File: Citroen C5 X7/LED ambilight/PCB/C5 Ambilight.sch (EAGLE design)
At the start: 21 parts, among them Q1 SQP90P06-07L_GE3, X1 2PIN_5MM_TERMINAL, X2 2PIN_5MM_TERMINAL, X3 JST-XH-03-PIN-ROUND-PAD

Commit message: Updated PCB
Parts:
- R2: value 12k -> 10k
- R3: value 470R -> 10k
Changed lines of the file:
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@@
 <grid distance="0.1" unitdist="inch" unit="inch" style="lines" multiple="1" display="no" altdistance="0.01" altunitdist="inch" altunit="inch"/>
 <layers>
-<layer number="1" name="Top" color="4" fill="1" visible="yes" active="no"/>
-<layer number="2" name="Route2" color="16" fill="1" visible="yes" active="no"/>
-<layer number="3" name="Route3" color="4" fill="3" visible="yes" active="no"/>
-<layer number="4" name="Route4" color="1" fill="4" visible="yes" active="no"/>
-<layer number="5" name="Route5" color="4" fill="4" visible="yes" active="no"/>
-<layer number="6" name="Route6" color="1" fill="8" visible="yes" active="no"/>
-<layer number="7" name="Route7" color="4" fill="8" visible="yes" active="no"/>
-<layer number="8" name="Route8" color="1" fill="2" visible="yes" active="no"/>
-<layer number="9" name="Route9" color="4" fill="2" visible="yes" active="no"/>
-<layer number="10" name="Route10" color="1" fill="7" visible="yes" active="no"/>
-<layer number="11" name="Route11" color="4" fill="7" visible="yes" active="no"/>
-<layer number="12" name="Route12" color="1" fill="5" visible="yes" active="no"/>
-<layer number="13" name="Route13" color="4" fill="5" visible="yes" active="no"/>
-<layer number="14" name="Route14" color="1" fill="6" visible="yes" active="no"/>
-<layer number="15" name="Route15" color="23" fill="1" visible="yes" active="no"/>
-<layer number="16" name="Bottom" color="1" fill="1" visible="yes" active="no"/>
-<layer number="17" name="Pads" color="2" fill="1" visible="yes" active="no"/>
-<layer number="18" name="Vias" color="2" fill="1" visible="yes" active="no"/>
-<layer number="19" name="Unrouted" color="6" fill="1" visible="yes" active="no"/>
-<layer number="20" name="Dimension" color="24" fill="1" visible="yes" active="no"/>
-<layer number="21" name="tPlace" color="7" fill="1" visible="yes" active="no"/>
-<layer number="22" name="bPlace" color="7" fill="1" visible="yes" active="no"/>
-<layer number="23" name="tOrigins" color="15" fill="1" visible="yes" active="no"/>
-<layer number="24" name="bOrigins" color="15" fill="1" visible="yes" active="no"/>
-<layer number="25" name="tNames" color="7" fill="1" visible="yes" active="no"/>
-<layer number="26" name="bNames" color="7" fill="1" visible="yes" active="no"/>
-<layer number="27" name="tValues" color="7" fill="1" visible="yes" active="no"/>
-<layer number="28" name="bValues" color="7" fill="1" visible="yes" active="no"/>
+<layer number="1" name="Top" color="4" fill="1" visible="no" active="no"/>
+<layer number="2" name="Route2" color="16" fill="1" visible="no" active="no"/>
+<layer number="3" name="Route3" color="4" fill="3" visible="no" active="no"/>
+<layer number="4" name="Route4" color="1" fill="4" visible="no" active="no"/>
+<layer number="5" name="Route5" color="4" fill="4" visible="no" active="no"/>
+<layer number="6" name="Route6" color="1" fill="8" visible="no" active="no"/>
+<layer number="7" name="Route7" color="4" fill="8" visible="no" active="no"/>
+<layer number="8" name="Route8" color="1" fill="2" visible="no" active="no"/>
+<layer number="9" name="Route9" color="4" fill="2" visible="no" active="no"/>
+<layer number="10" name="Route10" color="1" fill="7" visible="no" active="no"/>
+<layer number="11" name="Route11" color="4" fill="7" visible="no" active="no"/>
+<layer number="12" name="Route12" color="1" fill="5" visible="no" active="no"/>
+<layer number="13" name="Route13" color="4" fill="5" visible="no" active="no"/>
+<layer number="14" name="Route14" color="1" fill="6" visible="no" active="no"/>
+<layer number="15" name="Route15" color="23" fill="1" visible="no" active="no"/>
+<layer number="16" name="Bottom" color="1" fill="1" visible="no" active="no"/>
+<layer number="17" name="Pads" color="2" fill="1" visible="no" active="no"/>
+<layer number="18" name="Vias" color="2" fill="1" visible="no" active="no"/>
+<layer number="19" name="Unrouted" color="6" fill="1" visible="no" active="no"/>
+<layer number="20" name="Dimension" color="24" fill="1" visible="no" active="no"/>
+<layer number="21" name="tPlace" color="7" fill="1" visible="no" active="no"/>
+<layer number="22" name="bPlace" color="7" fill="1" visible="no" active="no"/>
+<layer number="23" name="tOrigins" color="15" fill="1" visible="no" active="no"/>
+<layer number="24" name="bOrigins" color="15" fill="1" visible="no" active="no"/>
+<layer number="25" name="tNames" color="7" fill="1" visible="no" active="no"/>
+<layer number="26" name="bNames" color="7" fill="1" visible="no" active="no"/>
+<layer number="27" name="tValues" color="7" fill="1" visible="no" active="no"/>
+<layer number="28" name="bValues" color="7" fill="1" visible="no" active="no"/>
 <layer number="29" name="tStop" color="7" fill="3" visible="no" active="no"/>
 <layer number="30" name="bStop" color="7" fill="6" visible="no" active="no"/>
@@
 <layer number="35" name="tGlue" color="7" fill="4" visible="no" active="no"/>
 <layer number="36" name="bGlue" color="7" fill="5" visible="no" active="no"/>
-<layer number="37" name="tTest" color="7" fill="1" visible="yes" active="no"/>
-<layer number="38" name="bTest" color="7" fill="1" visible="yes" active="no"/>
+<layer number="37" name="tTest" color="7" fill="1" visible="no" active="no"/>
+<layer number="38" name="bTest" color="7" fill="1" visible="no" active="no"/>
 <layer number="39" name="tKeepout" color="4" fill="11" visible="no" active="no"/>
 <layer number="40" name="bKeepout" color="1" fill="11" visible="no" active="no"/>
@@
 <layer number="44" name="Drills" color="7" fill="1" visible="no" active="no"/>
 <layer number="45" name="Holes" color="7" fill="1" visible="no" active="no"/>
-<layer number="46" name="Milling" color="3" fill="1" visible="yes" active="no"/>
-<layer number="47" name="Measures" color="7" fill="1" visible="yes" active="no"/>
-<layer number="48" name="Document" color="7" fill="1" visible="yes" active="no"/>
-<layer number="49" name="Reference" color="7" fill="1" visible="yes" active="no"/>
-<layer number="50" name="dxf" color="7" fill="1" visible="yes" active="no"/>
-<layer number="51" name="tDocu" color="7" fill="1" visible="yes" active="no"/>
-<layer number="52" name="bDocu" color="7" fill="1" visible="yes" active="no"/>
-<layer number="53" name="tGND_GNDA" color="7" fill="9" visible="yes" active="no"/>
-<layer number="54" name="bGND_GNDA" color="1" fill="9" visible="yes" active="no"/>
-<layer number="56" name="wert" color="7" fill="1" visible="yes" active="no"/>
-<layer number="57" name="tCAD" color="7" fill="1" visible="yes" active="no"/>
-<layer number="59" name="tCarbon" color="7" fill="1" visible="yes" active="no"/>
-<layer number="60" name="bCarbon" color="7" fill="1" visible="yes" active="no"/>
+<layer number="46" name="Milling" color="3" fill="1" visible="no" active="no"/>
+<layer number="47" name="Measures" color="7" fill="1" visible="no" active="no"/>
+<layer number="48" name="Document" color="7" fill="1" visible="no" active="no"/>
+<layer number="49" name="Reference" color="7" fill="1" visible="no" active="no"/>
+<layer number="50" name="dxf" color="7" fill="1" visible="no" active="no"/>
+<layer number="51" name="tDocu" color="7" fill="1" visible="no" active="no"/>
+<layer number="52" name="bDocu" color="7" fill="1" visible="no" active="no"/>
+<layer number="53" name="tGND_GNDA" color="7" fill="9" visible="no" active="no"/>
+<layer number="54" name="bGND_GNDA" color="1" fill="9" visible="no" active="no"/>
+<layer number="56" name="wert" color="7" fill="1" visible="no" active="no"/>
+<layer number="57" name="tCAD" color="7" fill="1" visible="no" active="no"/>
+<layer number="59" name="tCarbon" color="7" fill="1" visible="no" active="no"/>
+<layer number="60" name="bCarbon" color="7" fill="1" visible="no" active="no"/>
 <layer number="88" name="SimResults" color="9" fill="1" visible="yes" active="yes"/>
 <layer number="89" name="SimProbes" color="9" fill="1" visible="yes" active="yes"/>
@@
 <part name="OK2" library="optocoupler" deviceset="SFH618?*" device="A" package3d_urn="urn:adsk.eagle:package:21960/1" technology="-3"/>
 <part name="X2" library="Terminaly" deviceset="2PIN_5MM_TERMINAL" device=""/>
-<part name="R3" library="resistor" deviceset="R-EU_" device="0207/7" package3d_urn="urn:adsk.eagle:package:23493/1" value="470R"/>
-<part name="R2" library="resistor" deviceset="R-EU_" device="0207/7" package3d_urn="urn:adsk.eagle:package:23493/1" value="12k"/>
+<part name="R3" library="resistor" deviceset="R-EU_" device="0207/7" package3d_urn="urn:adsk.eagle:package:23493/1" value="10k"/>
+<part name="R2" library="resistor" deviceset="R-EU_" device="0207/7" package3d_urn="urn:adsk.eagle:package:23493/1" value="10k"/>
 <part name="R4" library="resistor" deviceset="R-EU_" device="0207/10" package3d_urn="urn:adsk.eagle:package:23491/1" value="10k"/>
 <part name="R5" library="resistor" deviceset="R-EU_" device="0207/10" package3d_urn="urn:adsk.eagle:package:23491/1" value="10k"/>

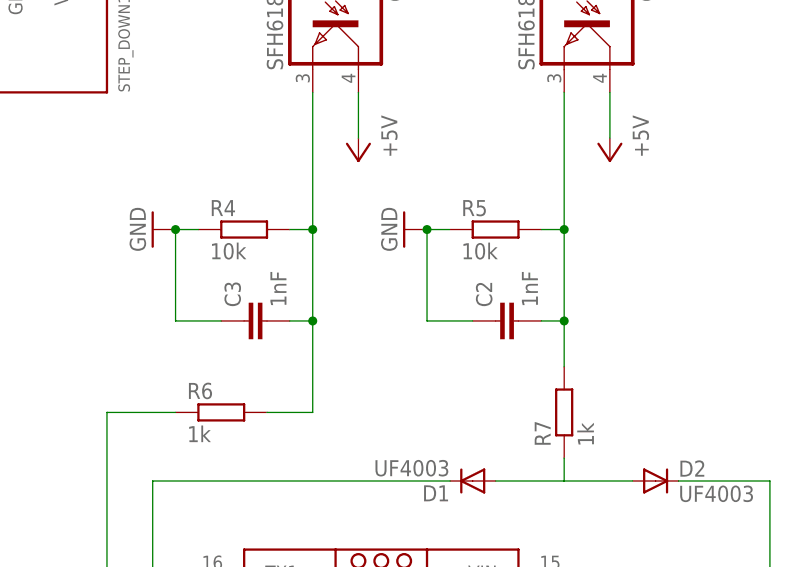
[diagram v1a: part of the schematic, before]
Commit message: Fix capacitor value
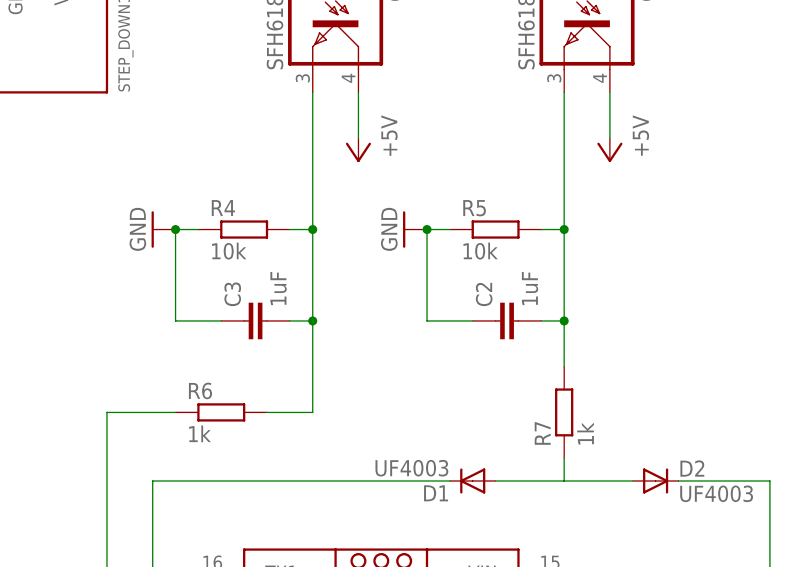
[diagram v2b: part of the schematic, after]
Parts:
- C2, C3: value 1nF -> 1uF
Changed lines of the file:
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@@
 <part name="GND5" library="supply1" deviceset="GND" device=""/>
 <part name="GND6" library="supply1" deviceset="GND" device=""/>
-<part name="C2" library="resistor" deviceset="C-EU" device="050-025X075" package3d_urn="urn:adsk.eagle:package:23637/1" value="1nF"/>
-<part name="C3" library="resistor" deviceset="C-EU" device="050-025X075" package3d_urn="urn:adsk.eagle:package:23637/1" value="1nF"/>
+<part name="C2" library="resistor" deviceset="C-EU" device="050-025X075" package3d_urn="urn:adsk.eagle:package:23637/1" value="1uF"/>
+<part name="C3" library="resistor" deviceset="C-EU" device="050-025X075" package3d_urn="urn:adsk.eagle:package:23637/1" value="1uF"/>
 <part name="GND7" library="supply1" deviceset="GND" device=""/>
 <part name="GND8" library="supply1" deviceset="GND" device=""/>
